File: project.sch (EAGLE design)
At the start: 6 parts, among them U1 DSPIC33FJ64MC804-H/PT

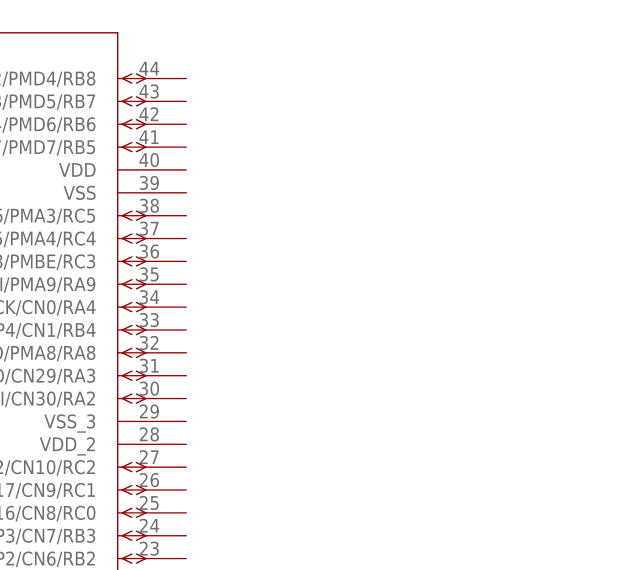
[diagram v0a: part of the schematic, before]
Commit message: add external oscillator
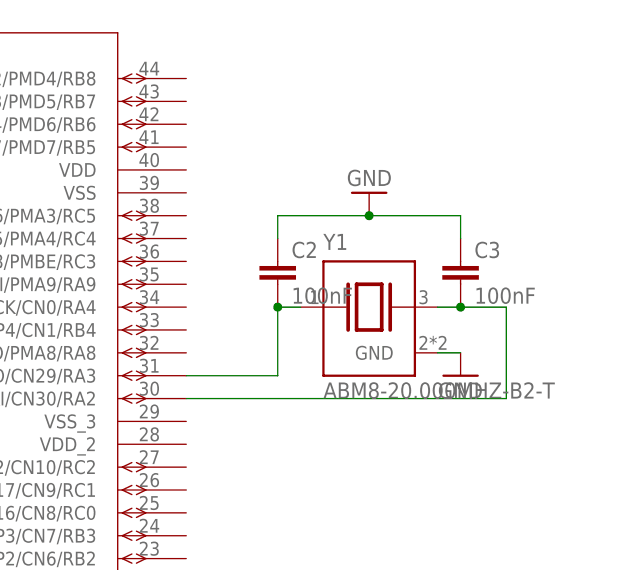
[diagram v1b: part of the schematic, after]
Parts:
- added C2, C3: 100nF, capacitor-wima:C2,5-3
- added Y1: ABM8-20.000MHZ-B2-T, ABM8-20.000MHZ-B2-T:ABM8-20.000MHZ-B2-T
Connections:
- new net N$1: C2.2, U1.OSC2/CLKO/CN29/RA3, Y1.1
- new net N$2: C3.2, U1.OSC1/CLKI/CN30/RA2, Y1.2
- net GND: now also C2.1, C3.1, Y1.GND
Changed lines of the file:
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@@
 <part name="GND2" library="supply1" library_urn="urn:adsk.eagle:library:371" deviceset="GND" device=""/>
 <part name="GND3" library="supply1" library_urn="urn:adsk.eagle:library:371" deviceset="GND" device=""/>
+<part name="Y1" library="ABM8-20.000MHZ-B2-T" deviceset="ABM8-20.000MHZ-B2-T" device=""/>
+<part name="GND4" library="supply1" library_urn="urn:adsk.eagle:library:371" deviceset="GND" device=""/>
+<part name="C2" library="capacitor-wima" library_urn="urn:adsk.eagle:library:116" deviceset="C" device="2,5-3" package3d_urn="urn:adsk.eagle:package:5436/1" value="100nF"/>
+<part name="C3" library="capacitor-wima" library_urn="urn:adsk.eagle:library:116" deviceset="C" device="2,5-3" package3d_urn="urn:adsk.eagle:package:5436/1" value="100nF"/>
+<part name="GND5" library="supply1" library_urn="urn:adsk.eagle:library:371" deviceset="GND" device=""/>
 </parts>
 <sheets>
@@
 <attribute name="VALUE" x="-104.14" y="-38.1" size="1.778" layer="96"/>
 </instance>
+<instance part="Y1" gate="G$1" x="144.78" y="0" smashed="yes">
+<attribute name="NAME" x="139.6922" y="6.35585" size="1.78073125" layer="95"/>
+<attribute name="VALUE" x="139.685609375" y="-10.16" size="1.78303125" layer="96"/>
+</instance>
+<instance part="GND4" gate="1" x="154.94" y="-7.62" smashed="yes">
+<attribute name="VALUE" x="152.4" y="-10.16" size="1.778" layer="96"/>
+</instance>
+<instance part="C2" gate="G$1" x="134.62" y="5.08" smashed="yes">
+<attribute name="NAME" x="136.144" y="5.461" size="1.778" layer="95"/>
+<attribute name="VALUE" x="136.144" y="0.381" size="1.778" layer="96"/>
+</instance>
+<instance part="C3" gate="G$1" x="154.94" y="5.08" smashed="yes">
+<attribute name="NAME" x="156.464" y="5.461" size="1.778" layer="95"/>
+<attribute name="VALUE" x="156.464" y="0.381" size="1.778" layer="96"/>
+</instance>
+<instance part="GND5" gate="1" x="144.78" y="12.7" smashed="yes" rot="R180">
+<attribute name="VALUE" x="147.32" y="15.24" size="1.778" layer="96" rot="R180"/>
+</instance>
 </instances>
 <busses>
@@
 <wire x1="-101.6" y1="-30.48" x2="-101.6" y2="-33.02" width="0.1524" layer="91"/>
 </segment>
+<segment>
+<pinref part="C2" gate="G$1" pin="1"/>
+<pinref part="GND5" gate="1" pin="GND"/>
+<wire x1="134.62" y1="7.62" x2="134.62" y2="10.16" width="0.1524" layer="91"/>
+<wire x1="134.62" y1="10.16" x2="144.78" y2="10.16" width="0.1524" layer="91"/>
+<pinref part="C3" gate="G$1" pin="1"/>
+<wire x1="144.78" y1="10.16" x2="154.94" y2="10.16" width="0.1524" layer="91"/>
+<wire x1="154.94" y1="10.16" x2="154.94" y2="7.62" width="0.1524" layer="91"/>
+<junction x="144.78" y="10.16"/>
+</segment>
+<segment>
+<pinref part="Y1" gate="G$1" pin="GND"/>
+<pinref part="GND4" gate="1" pin="GND"/>
+<wire x1="154.94" y1="-5.08" x2="152.4" y2="-5.08" width="0.1524" layer="91"/>
+</segment>
 </net>
 <net name="AN0" class="0">
@@
 </segment>
 </net>
+<net name="N$1" class="0">
+<segment>
+<pinref part="Y1" gate="G$1" pin="1"/>
+<pinref part="C2" gate="G$1" pin="2"/>
+<wire x1="137.16" y1="0" x2="134.62" y2="0" width="0.1524" layer="91"/>
+<wire x1="134.62" y1="0" x2="134.62" y2="-7.62" width="0.1524" layer="91"/>
+<junction x="134.62" y="0"/>
+<pinref part="U1" gate="A" pin="OSC2/CLKO/CN29/RA3"/>
+<wire x1="134.62" y1="-7.62" x2="124.46" y2="-7.62" width="0.1524" layer="91"/>
+</segment>
+</net>
+<net name="N$2" class="0">
+<segment>
+<pinref part="C3" gate="G$1" pin="2"/>
+<pinref part="Y1" gate="G$1" pin="2"/>
+<wire x1="154.94" y1="0" x2="152.4" y2="0" width="0.1524" layer="91"/>
+<pinref part="U1" gate="A" pin="OSC1/CLKI/CN30/RA2"/>
+<wire x1="124.46" y1="-10.16" x2="160.02" y2="-10.16" width="0.1524" layer="91"/>
+<wire x1="160.02" y1="-10.16" x2="160.02" y2="0" width="0.1524" layer="91"/>
+<wire x1="160.02" y1="0" x2="154.94" y2="0" width="0.1524" layer="91"/>
+<junction x="154.94" y="0"/>
+</segment>
+</net>

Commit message: connect the other 2 sensors
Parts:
- added C4, C5: 100nF, capacitor-wima:C2,5-3
- added R2, R3: 10k, rcl:R-EU_0204/2V
- added U2: TB6612FNG,C,8,EL, TB6612FNG_C_8_EL:TB6612FNG,C,8,EL
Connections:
- new net AN1: C4.1, JP2(GP2Y0A51SK0F).2, R2.2, U1.AN1/VREF-/CN3/RA1
- new net AN4: C5.1, JP3(GP2Y0A51SK0F).2, R3.2, U1.AN4/C1IN-/RP2/CN6/RB2
- net GND: now also C4.2, C5.2, JP2(GP2Y0A51SK0F).3, JP3(GP2Y0A51SK0F).3, R2.1, R3.1
- net VCC: now also JP2(GP2Y0A51SK0F).1, JP3(GP2Y0A51SK0F).1
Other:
- moved on the sheet: JP2(GP2Y0A51SK0F), JP3(GP2Y0A51SK0F)

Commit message: add motor driver
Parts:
- added C6, C8: 0.1uF, capacitor-wima:C2,5-3
- added C7, C9: 10uF, capacitor-wima:C2,5-3
- C2, C3: value 100nF -> 22pF
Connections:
- new net MTRDRV_AIN1: U2.AIN1
- new net MTRDRV_AIN2: U2.AIN2
- new net MTRDRV_BIN1: U2.BIN1
- new net MTRDRV_BIN2: U2.BIN2
- new net N$3: C8.1, C9.1, U2.VM1, U2.VM2, U2.VM3
- new net PWMA: U2.PWMA
- new net PWMB: U2.PWMB
- new net STBY: U2.STBY
- net GND: now also C6.2, C7.2, C8.2, C9.2
- net VCC: now also C6.1, C7.1, U2.VCC
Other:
- moved on the sheet: C1, C4, C5, JP1(GP2Y0A51SK0F), JP2(GP2Y0A51SK0F), JP3(GP2Y0A51SK0F), R1, R2, R3, U2

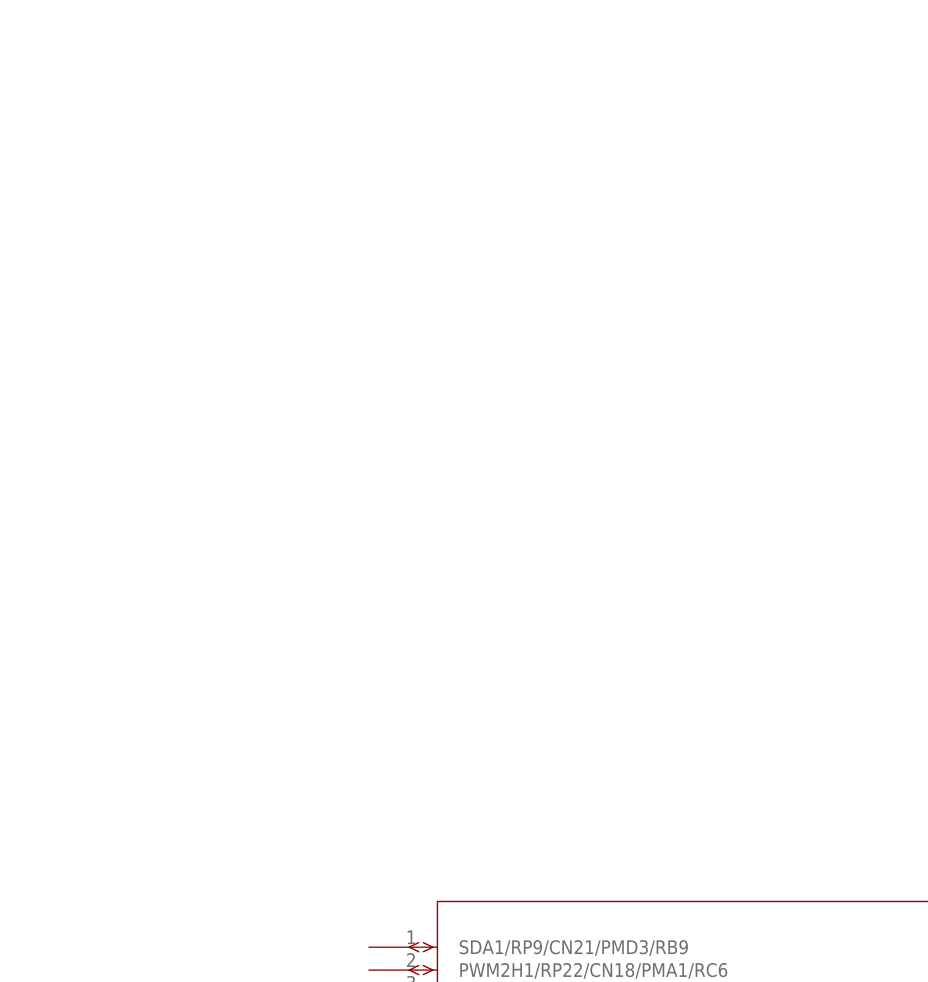
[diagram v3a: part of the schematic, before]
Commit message: add UAB_UART converter
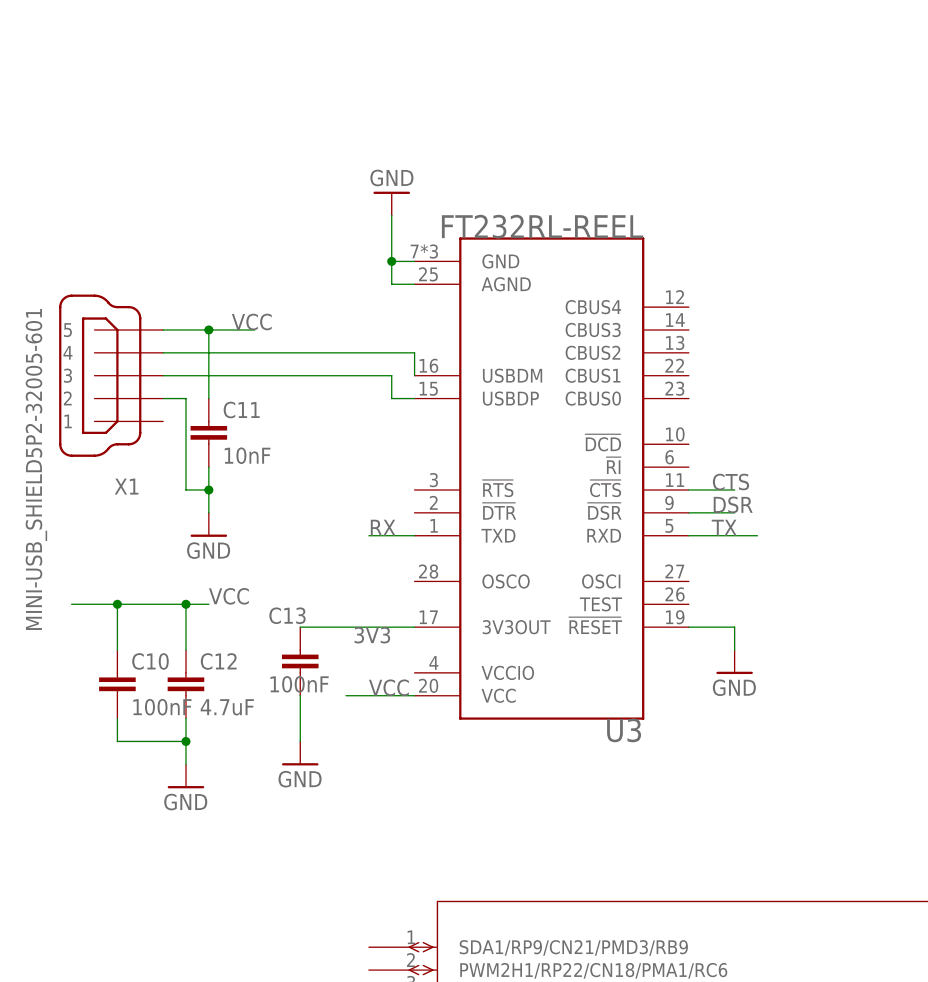
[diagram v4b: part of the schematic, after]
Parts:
- added C10, C13: 100nF, capacitor-wima:C2,5-3
- added C11: 10nF, capacitor-wima:C2,5-3
- added C12: 4.7uF, capacitor-wima:C2,5-3
- added U3: FT232RL-REEL, FT232RL-REEL:FT232RL-REEL
- added X1: MINI-USB_SHIELD5P2-32005-601, con-cypressindustries:MINI-USB_SHIELD5P2-32005-601
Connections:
- new net 3V3: C13.1, U3.3V3OUT
- new net CTS: U3.!CTS
- new net DSR: U3.!DSR
- new net N$4: U3.USBDM, X1G41.4
- new net N$5: U3.USBDP, X1G41.3
- new net RX: U3.TXD
- new net TX: U3.RXD
- net GND: now also C10.2, C11.2, C12.2, C13.2, U3.!RESET, U3.AGND, U3.GND, X1G41.2
- net VCC: now also C10.1, C11.1, C12.1, U3.VCC, X1G41.5
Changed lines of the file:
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@@
 <part name="C9" library="capacitor-wima" library_urn="urn:adsk.eagle:library:116" deviceset="C" device="2,5-3" package3d_urn="urn:adsk.eagle:package:5436/1" value="10uF"/>
 <part name="GND13" library="supply1" library_urn="urn:adsk.eagle:library:371" deviceset="GND" device=""/>
+<part name="U3" library="FT232RL-REEL" deviceset="FT232RL-REEL" device=""/>
+<part name="X1" library="con-cypressindustries" library_urn="urn:adsk.eagle:library:138" deviceset="MINI-USB_SHIELD5P2-" device="32005-601" package3d_urn="urn:adsk.eagle:package:6465/1"/>
+<part name="C11" library="capacitor-wima" library_urn="urn:adsk.eagle:library:116" deviceset="C" device="2,5-3" package3d_urn="urn:adsk.eagle:package:5436/1" value="10nF"/>
+<part name="GND14" library="supply1" library_urn="urn:adsk.eagle:library:371" deviceset="GND" device=""/>
+<part name="GND15" library="supply1" library_urn="urn:adsk.eagle:library:371" deviceset="GND" device=""/>
+<part name="GND16" library="supply1" library_urn="urn:adsk.eagle:library:371" deviceset="GND" device=""/>
+<part name="C10" library="capacitor-wima" library_urn="urn:adsk.eagle:library:116" deviceset="C" device="2,5-3" package3d_urn="urn:adsk.eagle:package:5436/1" value="100nF"/>
+<part name="C12" library="capacitor-wima" library_urn="urn:adsk.eagle:library:116" deviceset="C" device="2,5-3" package3d_urn="urn:adsk.eagle:package:5436/1" value="4.7uF"/>
+<part name="GND17" library="supply1" library_urn="urn:adsk.eagle:library:371" deviceset="GND" device=""/>
+<part name="C13" library="capacitor-wima" library_urn="urn:adsk.eagle:library:116" deviceset="C" device="2,5-3" package3d_urn="urn:adsk.eagle:package:5436/1" value="100nF"/>
+<part name="GND18" library="supply1" library_urn="urn:adsk.eagle:library:371" deviceset="GND" device=""/>
 </parts>
 <sheets>
@@
 <instance part="GND13" gate="1" x="165.1" y="88.9" smashed="yes">
 <attribute name="VALUE" x="162.56" y="86.36" size="1.778" layer="96"/>
+</instance>
+<instance part="U3" gate="G$1" x="-43.18" y="78.74" smashed="yes" rot="R180">
+<attribute name="VALUE" x="-33.0013" y="106.7315" size="2.54468125" layer="96" rot="R180"/>
+<attribute name="NAME" x="-33.0061" y="50.7618" size="2.54346875" layer="95" rot="R180"/>
+</instance>
+<instance part="X1" gate="G41" x="-91.44" y="88.9" smashed="yes" rot="R180">
+<attribute name="NAME" x="-88.9" y="77.47" size="1.778" layer="95" rot="R180"/>
+<attribute name="VALUE" x="-101.6" y="96.52" size="1.778" layer="96" rot="R270"/>
+</instance>
+<instance part="C11" gate="G$1" x="-81.28" y="83.82" smashed="yes">
+<attribute name="NAME" x="-79.756" y="84.201" size="1.778" layer="95"/>
+<attribute name="VALUE" x="-79.756" y="79.121" size="1.778" layer="96"/>
+</instance>
+<instance part="GND14" gate="1" x="-81.28" y="71.12" smashed="yes">
+<attribute name="VALUE" x="-83.82" y="68.58" size="1.778" layer="96"/>
+</instance>
+<instance part="GND15" gate="1" x="-60.96" y="109.22" smashed="yes" rot="R180">
+<attribute name="VALUE" x="-58.42" y="111.76" size="1.778" layer="96" rot="R180"/>
+</instance>
+<instance part="GND16" gate="1" x="-22.86" y="55.88" smashed="yes">
+<attribute name="VALUE" x="-25.4" y="53.34" size="1.778" layer="96"/>
+</instance>
+<instance part="C10" gate="G$1" x="-91.44" y="55.88" smashed="yes">
+<attribute name="NAME" x="-89.916" y="56.261" size="1.778" layer="95"/>
+<attribute name="VALUE" x="-89.916" y="51.181" size="1.778" layer="96"/>
+</instance>
+<instance part="C12" gate="G$1" x="-83.82" y="55.88" smashed="yes">
+<attribute name="NAME" x="-82.296" y="56.261" size="1.778" layer="95"/>
+<attribute name="VALUE" x="-82.296" y="51.181" size="1.778" layer="96"/>
+</instance>
+<instance part="GND17" gate="1" x="-83.82" y="43.18" smashed="yes">
+<attribute name="VALUE" x="-86.36" y="40.64" size="1.778" layer="96"/>
+</instance>
+<instance part="C13" gate="G$1" x="-71.12" y="58.42" smashed="yes">
+<attribute name="NAME" x="-74.676" y="61.341" size="1.778" layer="95"/>
+<attribute name="VALUE" x="-74.676" y="53.721" size="1.778" layer="96"/>
+</instance>
+<instance part="GND18" gate="1" x="-71.12" y="45.72" smashed="yes">
+<attribute name="VALUE" x="-73.66" y="43.18" size="1.778" layer="96"/>
 </instance>
 </instances>
@@
 <junction x="142.24" y="129.54"/>
 </segment>
+<segment>
+<pinref part="X1" gate="G41" pin="5"/>
+<label x="-78.74" y="93.98" size="1.778" layer="95"/>
+<wire x1="-86.36" y1="93.98" x2="-81.28" y2="93.98" width="0.1524" layer="91"/>
+<wire x1="-76.2" y1="93.98" x2="-81.28" y2="93.98" width="0.1524" layer="91"/>
+<pinref part="C11" gate="G$1" pin="1"/>
+<wire x1="-81.28" y1="86.36" x2="-81.28" y2="93.98" width="0.1524" layer="91"/>
+<junction x="-81.28" y="93.98"/>
+</segment>
+<segment>
+<pinref part="U3" gate="G$1" pin="VCC"/>
+<wire x1="-58.42" y1="53.34" x2="-66.04" y2="53.34" width="0.1524" layer="91"/>
+<label x="-63.5" y="53.34" size="1.778" layer="95"/>
+</segment>
+<segment>
+<wire x1="-96.52" y1="63.5" x2="-91.44" y2="63.5" width="0.1524" layer="91"/>
+<wire x1="-91.44" y1="63.5" x2="-83.82" y2="63.5" width="0.1524" layer="91"/>
+<wire x1="-83.82" y1="63.5" x2="-81.28" y2="63.5" width="0.1524" layer="91"/>
+<wire x1="-91.44" y1="63.5" x2="-91.44" y2="58.42" width="0.1524" layer="91"/>
+<junction x="-91.44" y="63.5"/>
+<wire x1="-83.82" y1="63.5" x2="-83.82" y2="58.42" width="0.1524" layer="91"/>
+<junction x="-83.82" y="63.5"/>
+<pinref part="C10" gate="G$1" pin="1"/>
+<pinref part="C12" gate="G$1" pin="1"/>
+<label x="-81.28" y="63.5" size="1.778" layer="95"/>
+</segment>
 </net>
 <net name="GND" class="0">
@@
 <junction x="165.1" y="91.44"/>
 <pinref part="GND13" gate="1" pin="GND"/>
+</segment>
+<segment>
+<pinref part="X1" gate="G41" pin="2"/>
+<wire x1="-86.36" y1="86.36" x2="-83.82" y2="86.36" width="0.1524" layer="91"/>
+<wire x1="-83.82" y1="86.36" x2="-83.82" y2="76.2" width="0.1524" layer="91"/>
+<wire x1="-83.82" y1="76.2" x2="-81.28" y2="76.2" width="0.1524" layer="91"/>
+<pinref part="C11" gate="G$1" pin="2"/>
+<wire x1="-81.28" y1="76.2" x2="-81.28" y2="78.74" width="0.1524" layer="91"/>
+<wire x1="-81.28" y1="76.2" x2="-81.28" y2="73.66" width="0.1524" layer="91"/>
+<junction x="-81.28" y="76.2"/>
+<pinref part="GND14" gate="1" pin="GND"/>
+</segment>
+<segment>
+<pinref part="U3" gate="G$1" pin="GND"/>
+<wire x1="-58.42" y1="101.6" x2="-60.96" y2="101.6" width="0.1524" layer="91"/>
+<pinref part="GND15" gate="1" pin="GND"/>
+<wire x1="-60.96" y1="101.6" x2="-60.96" y2="106.68" width="0.1524" layer="91"/>
+<pinref part="U3" gate="G$1" pin="AGND"/>
+<wire x1="-58.42" y1="99.06" x2="-60.96" y2="99.06" width="0.1524" layer="91"/>
+<wire x1="-60.96" y1="99.06" x2="-60.96" y2="101.6" width="0.1524" layer="91"/>
+<junction x="-60.96" y="101.6"/>
+</segment>
+<segment>
+<pinref part="U3" gate="G$1" pin="!RESET"/>
+<pinref part="GND16" gate="1" pin="GND"/>
+<wire x1="-27.94" y1="60.96" x2="-22.86" y2="60.96" width="0.1524" layer="91"/>
+<wire x1="-22.86" y1="60.96" x2="-22.86" y2="58.42" width="0.1524" layer="91"/>
+</segment>
+<segment>
+<pinref part="C10" gate="G$1" pin="2"/>
+<wire x1="-91.44" y1="50.8" x2="-91.44" y2="48.26" width="0.1524" layer="91"/>
+<wire x1="-91.44" y1="48.26" x2="-83.82" y2="48.26" width="0.1524" layer="91"/>
+<pinref part="C12" gate="G$1" pin="2"/>
+<wire x1="-83.82" y1="48.26" x2="-83.82" y2="50.8" width="0.1524" layer="91"/>
+<wire x1="-83.82" y1="48.26" x2="-83.82" y2="45.72" width="0.1524" layer="91"/>
+<junction x="-83.82" y="48.26"/>
+<pinref part="GND17" gate="1" pin="GND"/>
+</segment>
+<segment>
+<pinref part="C13" gate="G$1" pin="2"/>
+<wire x1="-71.12" y1="53.34" x2="-71.12" y2="48.26" width="0.1524" layer="91"/>
+<pinref part="GND18" gate="1" pin="GND"/>
 </segment>
 </net>
@@
 </segment>
 </net>
+<net name="N$4" class="0">
+<segment>
+<pinref part="X1" gate="G41" pin="4"/>
+<pinref part="U3" gate="G$1" pin="USBDM"/>
+<wire x1="-86.36" y1="91.44" x2="-58.42" y2="91.44" width="0.1524" layer="91"/>
+<wire x1="-58.42" y1="91.44" x2="-58.42" y2="88.9" width="0.1524" layer="91"/>
+</segment>
+</net>
+<net name="N$5" class="0">
+<segment>
+<pinref part="X1" gate="G41" pin="3"/>
+<wire x1="-86.36" y1="88.9" x2="-60.96" y2="88.9" width="0.1524" layer="91"/>
+<wire x1="-60.96" y1="88.9" x2="-60.96" y2="86.36" width="0.1524" layer="91"/>
+<pinref part="U3" gate="G$1" pin="USBDP"/>
+<wire x1="-60.96" y1="86.36" x2="-58.42" y2="86.36" width="0.1524" layer="91"/>
+</segment>
+</net>
+<net name="3V3" class="0">
+<segment>
+<pinref part="U3" gate="G$1" pin="3V3OUT"/>
+<pinref part="C13" gate="G$1" pin="1"/>
+<wire x1="-58.42" y1="60.96" x2="-71.12" y2="60.96" width="0.1524" layer="91"/>
+<label x="-60.96" y="60.96" size="1.778" layer="95" rot="R180"/>
+</segment>
+</net>
+<net name="TX" class="0">
+<segment>
+<pinref part="U3" gate="G$1" pin="RXD"/>
+<wire x1="-27.94" y1="71.12" x2="-20.32" y2="71.12" width="0.1524" layer="91"/>
+<label x="-25.4" y="71.12" size="1.778" layer="95"/>
+</segment>
+</net>
+<net name="CTS" class="0">
+<segment>
+<pinref part="U3" gate="G$1" pin="!CTS"/>
+<wire x1="-27.94" y1="76.2" x2="-22.86" y2="76.2" width="0.1524" layer="91"/>
+<label x="-25.4" y="76.2" size="1.778" layer="95"/>
+</segment>
+</net>
+<net name="DSR" class="0">
+<segment>
+<pinref part="U3" gate="G$1" pin="!DSR"/>
+<wire x1="-27.94" y1="73.66" x2="-22.86" y2="73.66" width="0.1524" layer="91"/>
+<label x="-25.4" y="73.66" size="1.778" layer="95"/>
+</segment>
+</net>
+<net name="RX" class="0">
+<segment>
+<pinref part="U3" gate="G$1" pin="TXD"/>
+<wire x1="-58.42" y1="71.12" x2="-63.5" y2="71.12" width="0.1524" layer="91"/>
+<label x="-63.5" y="71.12" size="1.778" layer="95"/>
+</segment>
+</net>
